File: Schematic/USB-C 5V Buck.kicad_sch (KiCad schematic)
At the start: 36 parts, among them J10 5V_SYNC_MODES, Q25 CSD19531Q5A, Q26 CSD19531Q5A, U14 LM25190RGYR

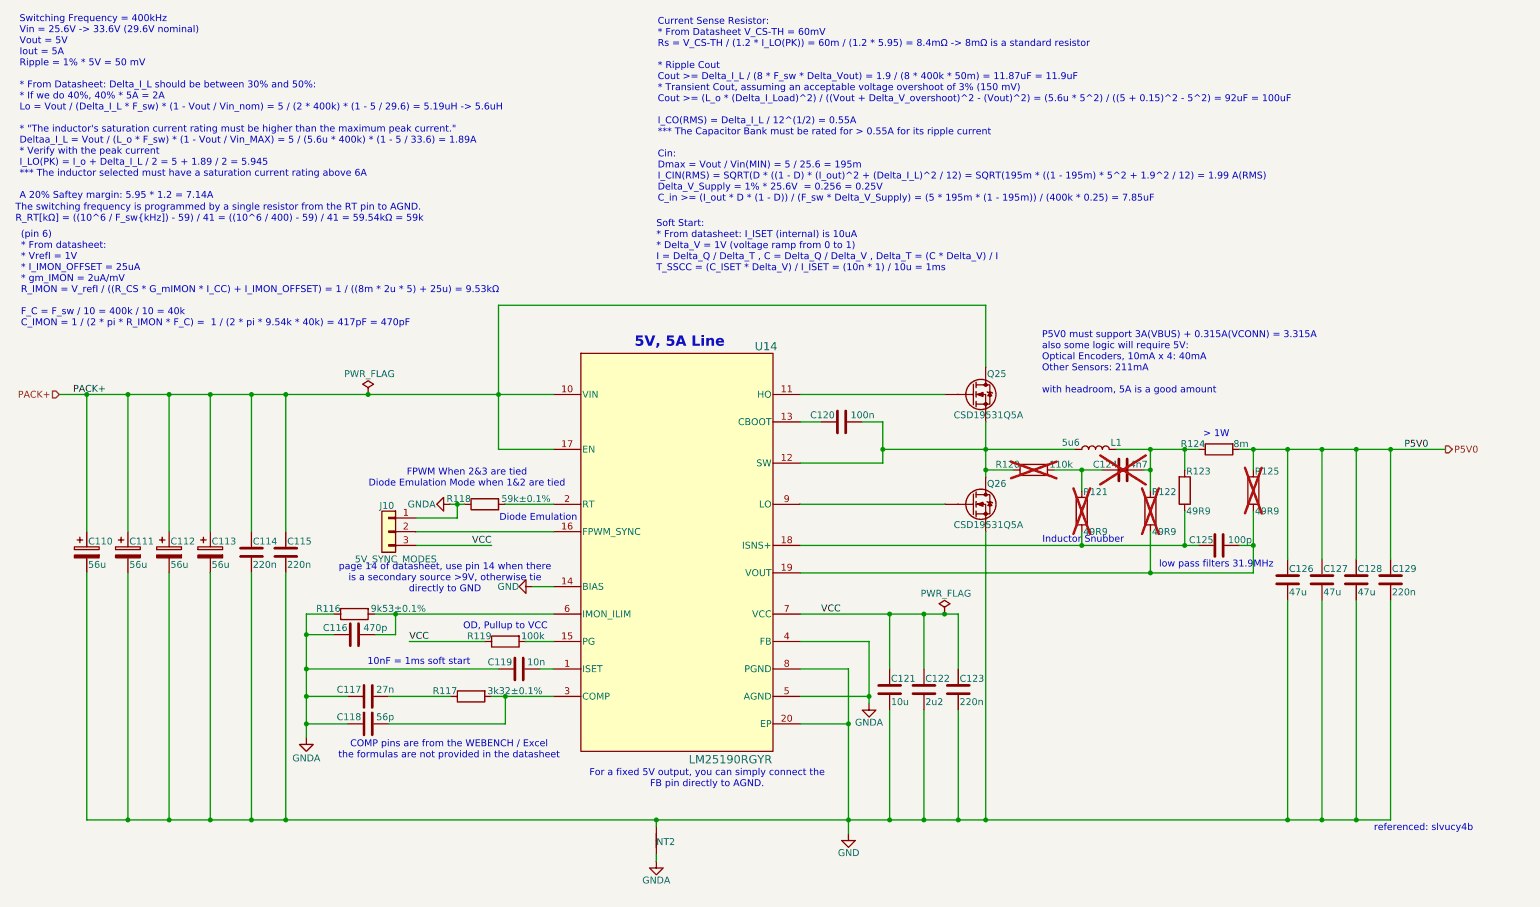
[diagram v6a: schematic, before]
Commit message: Added MCU
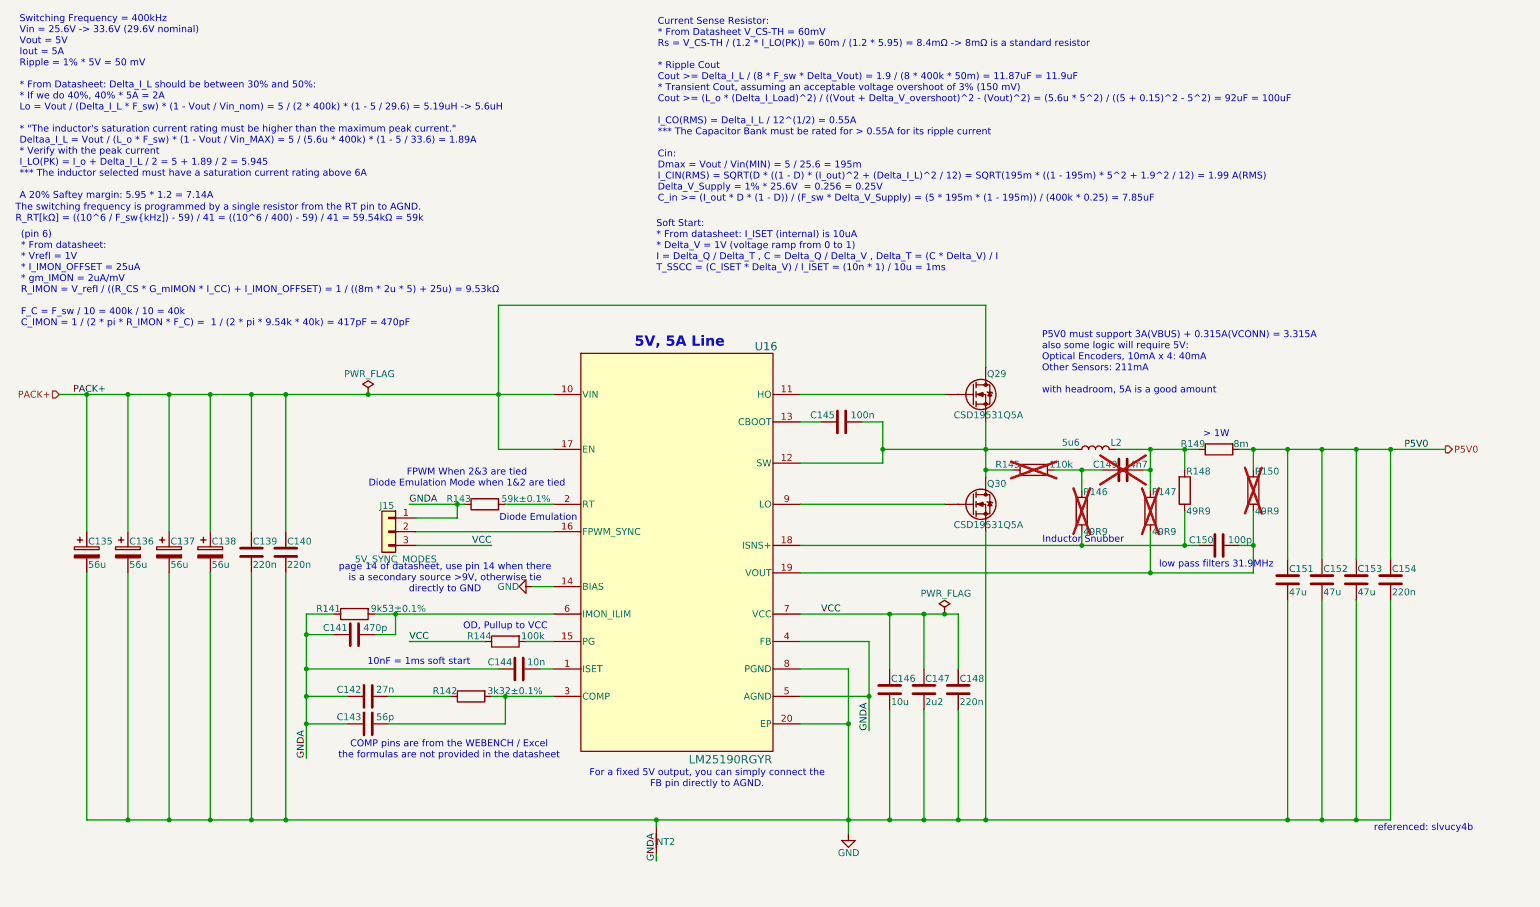
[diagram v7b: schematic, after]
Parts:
- renumbered C110 to C135, C111 to C136, C112 to C137, C113 to C138, C114 to C139, C115 to C140, C116 to C141, C117 to C142, C118 to C143, C119 to C144, C120 to C145, C121 to C146, C122 to C147, C123 to C148, C124 to C149, C125 to C150, C126 to C151, C127 to C152, C128 to C153, C129 to C154, J10 to J15, L1 to L2, Q25 to Q29, Q26 to Q30, R116 to R141, R117 to R142, R118 to R143, R119 to R144, R120 to R145, R121 to R146, R122 to R147, R123 to R148, R124 to R149, R125 to R150, U14 to U16

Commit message: Started to work on the BOM
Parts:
- removed C151, C152, C153: 47u, symbol Device:C
- added C150, C151, C152: 56u, AHA0810560M040R:CAPAE830X1100M, symbol Device:C_Polarized
- C134: renamed from C135; footprint (none) -> AHA0810560M040R:CAPAE830X1100M; Link (none) -> https://mou.sr/4g6lc2W; Manufacturer Part Number (none) -> AHA0810560M040R; Price per Unit (none) -> 1.50; Supplier (none) -> Mouser; Supplier Part Number (none) -> 581-AHA0810560M040R
- C135: renamed from C136; footprint (none) -> AHA0810560M040R:CAPAE830X1100M; Link (none) -> https://mou.sr/4g6lc2W; Manufacturer Part Number (none) -> AHA0810560M040R; Price per Unit (none) -> 1.50; Supplier (none) -> Mouser; Supplier Part Number (none) -> 581-AHA0810560M040R
- C136: renamed from C137; footprint (none) -> AHA0810560M040R:CAPAE830X1100M; Link (none) -> https://mou.sr/4g6lc2W; Manufacturer Part Number (none) -> AHA0810560M040R; Price per Unit (none) -> 1.50; Supplier (none) -> Mouser; Supplier Part Number (none) -> 581-AHA0810560M040R
- C137: renamed from C138; footprint (none) -> AHA0810560M040R:CAPAE830X1100M; Link (none) -> https://mou.sr/4g6lc2W; Manufacturer Part Number (none) -> AHA0810560M040R; Price per Unit (none) -> 1.50; Supplier (none) -> Mouser; Supplier Part Number (none) -> 581-AHA0810560M040R
- C138: renamed from C139; footprint (none) -> Capacitor_SMD:C_0805_2012Metric_Pad1.18x1.45mm_HandSolder; Link (none) -> https://mou.sr/42gipOV; Manufacturer Part Number (none) -> CL21B224KBFNFNE; Price per Unit (none) -> 0.10; Supplier (none) -> Mouser; Supplier Part Number (none) -> 187-CL21B224KBFNFNE
- C139: renamed from C140; footprint (none) -> Capacitor_SMD:C_0805_2012Metric_Pad1.18x1.45mm_HandSolder; Link (none) -> https://mou.sr/42gipOV; Manufacturer Part Number (none) -> CL21B224KBFNFNE; Price per Unit (none) -> 0.10; Supplier (none) -> Mouser; Supplier Part Number (none) -> 187-CL21B224KBFNFNE
- C140: renamed from C141; footprint (none) -> Capacitor_SMD:C_0603_1608Metric_Pad1.08x0.95mm_HandSolder; Link (none) -> https://mou.sr/3UXYSz1; Manufacturer Part Number (none) -> CL10C471JB8NNND; Price per Unit (none) -> 0.10; Supplier (none) -> Mouser; Supplier Part Number (none) -> 187-CL10C471JB8NNND
- C141: renamed from C142; value 27n -> 82n; footprint (none) -> Capacitor_SMD:C_1206_3216Metric_Pad1.33x1.80mm_HandSolder; Link (none) -> https://mou.sr/4m3RZXQ; Manufacturer Part Number (none) -> GRM3195C2A823GA01D; Price per Unit (none) -> 0.66; Supplier (none) -> Mouser; Supplier Part Number (none) -> 81-GRM3195C2A823GA1D
- C142: renamed from C143; footprint (none) -> Capacitor_SMD:C_0603_1608Metric_Pad1.08x0.95mm_HandSolder; Link (none) -> https://mou.sr/3JNA7TC; Manufacturer Part Number (none) -> CL10C560JB81PNC; Price per Unit (none) -> 0.10; Supplier (none) -> Mouser; Supplier Part Number (none) -> 187-CL10C560JB81PNC
- C143: renamed from C144; footprint (none) -> Capacitor_SMD:C_1206_3216Metric_Pad1.33x1.80mm_HandSolder; Link (none) -> https://mou.sr/3OC0xXF; Manufacturer Part Number (none) -> CL31B103KHFNFNE; Price per Unit (none) -> 0.13; Supplier (none) -> Mouser; Supplier Part Number (none) -> 187-CL31B103KHFNFNE
- C144: renamed from C145; footprint (none) -> Capacitor_SMD:C_1206_3216Metric_Pad1.33x1.80mm_HandSolder; Link (none) -> https://mou.sr/4n9ybmQ; Manufacturer Part Number (none) -> CL31B104KBCNNNC; Price per Unit (none) -> 0.11; Supplier (none) -> Mouser; Supplier Part Number (none) -> 187-CL31B104KBCNNNC
- C145: renamed from C146; footprint (none) -> Capacitor_SMD:C_1206_3216Metric_Pad1.33x1.80mm_HandSolder; Link (none) -> https://mou.sr/4l54Mdx; Manufacturer Part Number (none) -> CL31A106KBHNNNE; Price per Unit (none) -> 0.11; Supplier (none) -> Mouser; Supplier Part Number (none) -> 187-CL31A106KBHNNNE
- C146: renamed from C147; footprint (none) -> Capacitor_SMD:C_1206_3216Metric_Pad1.33x1.80mm_HandSolder; Link (none) -> https://mou.sr/3VA1gvS; Manufacturer Part Number (none) -> CL31A225KB9LNNC; Price per Unit (none) -> 0.15; Supplier (none) -> Mouser; Supplier Part Number (none) -> 187-CL31A225KB9LNNC
- C147: renamed from C148; footprint (none) -> Capacitor_SMD:C_0805_2012Metric_Pad1.18x1.45mm_HandSolder; Link (none) -> https://mou.sr/42gipOV; Manufacturer Part Number (none) -> CL21B224KBFNFNE; Price per Unit (none) -> 0.10; Supplier (none) -> Mouser; Supplier Part Number (none) -> 187-CL21B224KBFNFNE
- C148: renamed from C149; footprint (none) -> Capacitor_SMD:C_0603_1608Metric_Pad1.08x0.95mm_HandSolder; Link (none) -> https://mou.sr/4g6fuOy; Manufacturer Part Number (none) -> CL10B472KB8NFNC; Price per Unit (none) -> 0.10; Supplier (none) -> Mouser; Supplier Part Number (none) -> 187-CL10B472KB8NFNC
- C149: renamed from C150; footprint (none) -> Capacitor_SMD:C_0603_1608Metric_Pad1.08x0.95mm_HandSolder; Link (none) -> https://mou.sr/4kcxpDX; Manufacturer Part Number (none) -> CL10C101JB8NNNC; Price per Unit (none) -> 0.10; Supplier (none) -> Mouser; Supplier Part Number (none) -> 187-CL10C101JB8NNNC
- C153: renamed from C154; footprint (none) -> Capacitor_SMD:C_0805_2012Metric_Pad1.18x1.45mm_HandSolder; Link (none) -> https://mou.sr/42gipOV; Manufacturer Part Number (none) -> CL21B224KBFNFNE; Price per Unit (none) -> 0.10; Supplier (none) -> Mouser; Supplier Part Number (none) -> 187-CL21B224KBFNFNE
- Q29, Q30: footprint Package_TO_SOT_SMD:TDSON-8-1 -> (none)
- R138: renamed from R142; value 3k32±0.1% -> 1k78±0.1%
- U14: renamed from U16; footprint RGY0019C-MFG -> (none)
- renumbered J15 to J13, R141 to R137, R143 to R139, R144 to R140, R145 to R141, R146 to R142, R147 to R143, R148 to R144, R149 to R145, R150 to R146
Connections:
- net GND: now also C150.2, C151.2, C152.2
- net P5V0: now also C150.1, C151.1, C152.1
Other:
- moved on the sheet: C153
